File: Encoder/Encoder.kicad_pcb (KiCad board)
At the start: 2 copper layers, 10 parts, among them J1 Conn_01x04_Socket, J2 Conn_01x04_Socket

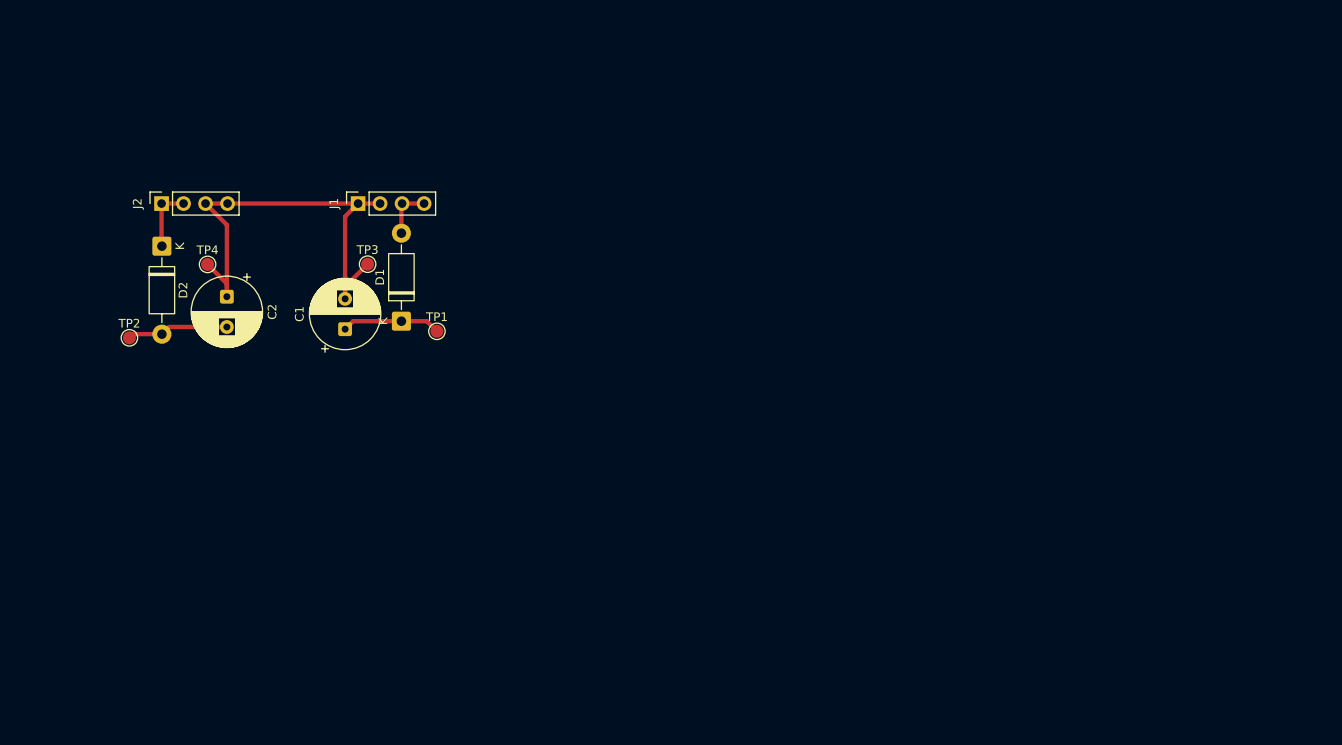
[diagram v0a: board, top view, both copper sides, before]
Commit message: added the filter for L and R
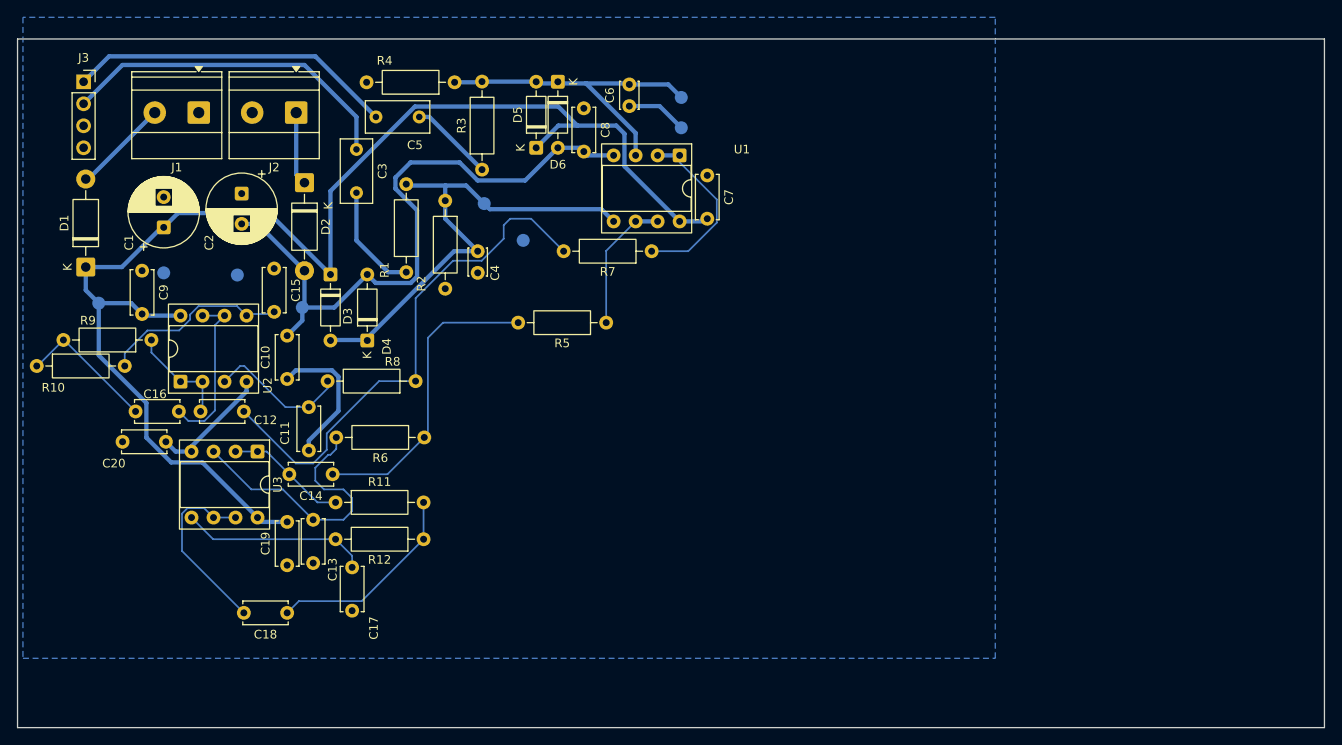
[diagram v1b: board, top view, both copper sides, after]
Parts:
- removed TP1, TP2, TP3, TP4: TestPoint, TestPoint:TestPoint_Pad_D1.5mm
- added C10: 100n, Capacitor_THT:C_Disc_D5.0mm_W2.5mm_P5.00mm, F.Cu at (37.5, 48.2)
- added C11: 1 n, Capacitor_THT:C_Disc_D5.0mm_W2.5mm_P5.00mm, F.Cu at (40.0, 56.5)
- added C12: 1 n, Capacitor_THT:C_Disc_D5.0mm_W2.5mm_P5.00mm, F.Cu at (32.5, 52.0)
- added C13: 1 n, Capacitor_THT:C_Disc_D5.0mm_W2.5mm_P5.00mm, F.Cu at (40.5, 69.5)
- added C14: 1 n, Capacitor_THT:C_Disc_D5.0mm_W2.5mm_P5.00mm, F.Cu at (42.8, 59.2)
- added C15: 330 p, Capacitor_THT:C_Disc_D5.0mm_W2.5mm_P5.00mm, F.Cu at (36.0, 35.5)
- added C16: 2.2 n, Capacitor_THT:C_Disc_D5.0mm_W2.5mm_P5.00mm, F.Cu at (20.0, 52.0)
- added C17: 330 p, Capacitor_THT:C_Disc_D5.0mm_W2.5mm_P5.00mm, F.Cu at (45.0, 75.0)
- added C18: 2.2 n, Capacitor_THT:C_Disc_D5.0mm_W2.5mm_P5.00mm, F.Cu at (37.5, 75.2)
- added C19: 100n, Capacitor_THT:C_Disc_D5.0mm_W2.5mm_P5.00mm, F.Cu at (37.5, 69.8)
- added C20: 100n, Capacitor_THT:C_Disc_D5.0mm_W2.5mm_P5.00mm, F.Cu at (18.5, 55.5)
- added C3: 1u, Capacitor_THT:C_Rect_L7.2mm_W3.5mm_P5.00mm, F.Cu at (45.5, 21.8)
- added C4: 100p, Capacitor_THT:C_Disc_D3.0mm_W2.0mm_P2.50mm, F.Cu at (59.5, 36.0)
- added C5: 1u, Capacitor_THT:C_Rect_L7.2mm_W3.5mm_P5.00mm, F.Cu at (47.8, 18.0)
- added C6: 100p, Capacitor_THT:C_Disc_D3.0mm_W2.0mm_P2.50mm, F.Cu at (77.0, 16.8)
- added C7: 100n, Capacitor_THT:C_Disc_D5.0mm_W2.5mm_P5.00mm, F.Cu at (86.0, 24.8)
- added C8: 100n, Capacitor_THT:C_Disc_D5.0mm_W2.5mm_P5.00mm, F.Cu at (71.8, 17.0)
- added C9: 100n, Capacitor_THT:C_Disc_D5.0mm_W2.5mm_P5.00mm, F.Cu at (20.8, 35.8)
- added D3: 1N4148, Diode_THT:D_DO-35_SOD27_P7.62mm_Horizontal, F.Cu at (42.5, 36.2)
- added D4: 1N4148, Diode_THT:D_DO-35_SOD27_P7.62mm_Horizontal, F.Cu at (46.8, 43.8)
- added D5: 1N4148, Diode_THT:D_DO-35_SOD27_P7.62mm_Horizontal, F.Cu at (66.2, 21.6)
- added D6: 1N4148, Diode_THT:D_DO-35_SOD27_P7.62mm_Horizontal, F.Cu at (68.8, 13.9)
- added J3: Conn_01x04_Socket, Connector_PinSocket_2.54mm:PinSocket_1x04_P2.54mm_Vertical, F.Cu at (14.0, 13.9)
- added R1: 10k, Resistor_THT:R_Axial_DIN0207_L6.3mm_D2.5mm_P10.16mm_Horizontal, F.Cu at (51.2, 35.9)
- added R10: 12k, Resistor_THT:R_Axial_DIN0207_L6.3mm_D2.5mm_P10.16mm_Horizontal, F.Cu at (8.59, 46.8)
- added R11: 12k, Resistor_THT:R_Axial_DIN0207_L6.3mm_D2.5mm_P10.16mm_Horizontal, F.Cu at (43.1, 62.5)
- added R12: 12k, Resistor_THT:R_Axial_DIN0207_L6.3mm_D2.5mm_P10.16mm_Horizontal, F.Cu at (53.2, 66.8)
- added R2: 100k, Resistor_THT:R_Axial_DIN0207_L6.3mm_D2.5mm_P10.16mm_Horizontal, F.Cu at (55.8, 27.7)
- added R3: 10k, Resistor_THT:R_Axial_DIN0207_L6.3mm_D2.5mm_P10.16mm_Horizontal, F.Cu at (60.0, 24.1)
- added R4: 100k, Resistor_THT:R_Axial_DIN0207_L6.3mm_D2.5mm_P10.16mm_Horizontal, F.Cu at (56.8, 14.0)
- added R5: 10k, Resistor_THT:R_Axial_DIN0207_L6.3mm_D2.5mm_P10.16mm_Horizontal, F.Cu at (74.3, 41.8)
- added R6: 10k, Resistor_THT:R_Axial_DIN0207_L6.3mm_D2.5mm_P10.16mm_Horizontal, F.Cu at (53.3, 55.0)
- added R7: 10k, Resistor_THT:R_Axial_DIN0207_L6.3mm_D2.5mm_P10.16mm_Horizontal, F.Cu at (79.6, 33.5)
- added R8: 10k, Resistor_THT:R_Axial_DIN0207_L6.3mm_D2.5mm_P10.16mm_Horizontal, F.Cu at (52.3, 48.5)
- added R9: 12k, Resistor_THT:R_Axial_DIN0207_L6.3mm_D2.5mm_P10.16mm_Horizontal, F.Cu at (21.8, 43.8)
- added TP_+9V1: TestPoint, TestPoint:TestPoint_Pad_D1.5mm, B.Cu at (15.8, 39.5)
- added TP_-9V1: TestPoint, TestPoint:TestPoint_Pad_D1.5mm, B.Cu at (39.2, 40.0)
- added TP_GND1: TestPoint, TestPoint:TestPoint_Pad_D1.5mm, B.Cu at (31.8, 36.2)
- added TP_GND2: TestPoint, TestPoint:TestPoint_Pad_D1.5mm, B.Cu at (64.8, 32.2)
- added TP_GND3: TestPoint, TestPoint:TestPoint_Pad_D1.5mm, B.Cu at (23.2, 36.0)
- added TP_GND4: TestPoint, TestPoint:TestPoint_Pad_D1.5mm, B.Cu at (83.0, 19.2)
- added TP_L1: TestPoint, TestPoint:TestPoint_Pad_D1.5mm, B.Cu at (83.0, 15.8)
- added TP_R1: TestPoint, TestPoint:TestPoint_Pad_D1.5mm, B.Cu at (60.2, 28.0)
- added U1: TL072, Package_DIP:DIP-8_W7.62mm_Socket, F.Cu at (82.8, 22.4)
- added U2: TL072, Package_DIP:DIP-8_W7.62mm_Socket, F.Cu at (25.2, 48.6)
- added U3: TL072, Package_DIP:DIP-8_W7.62mm_Socket, F.Cu at (34.1, 56.6)
- J1, J2: value Conn_01x04_Socket -> Conn_01x02_Socket; footprint Connector_PinSocket_2.54mm:PinSocket_1x04_P2.54mm_Vertical -> TerminalBlock_Phoenix:TerminalBlock_Phoenix_MKDS-1,5-2-5.08_1x02_P5.08mm_Horizontal
- moved D1 37.0 mm to (14.2, 35.3)
- moved C1 24.0 mm to (23.2, 30.8)
- moved J1 21.2 mm to (27.3, 17.5), turned to 180 degrees
- moved J2 18.8 mm to (38.5, 17.5), turned to 180 degrees
- moved D2 18.0 mm to (39.5, 25.6)
- moved C2 12.0 mm to (32.2, 26.8)
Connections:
- J1 pad 2: GND -> Net-(D1-A)
- J2 pad 2: Net-(D2-K) -> GND
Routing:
- net +9V: track 11.5 -> 157.5 mm
- net -9V: track 11.8 -> 88.7 mm
- net Net-(C12-Pad1): track 0.00 -> 60.3 mm
- net /right: track 0.00 -> 56.3 mm
- net Net-(J3-Pin_2): track 0.00 -> 39.6 mm
- net Net-(J3-Pin_1): track 0.00 -> 37.9 mm
- net /left: track 0.00 -> 37.7 mm
- net Net-(C14-Pad1): track 0.00 -> 35.2 mm
- net Net-(U3A-+): track 0.00 -> 32.4 mm
- net GND: track 53.3 -> 23.6 mm
- net Net-(C18-Pad1): track 0.00 -> 23.5 mm
- net Net-(U2B-+): track 0.00 -> 22.1 mm
- net Net-(U3B-+): track 0.00 -> 21.7 mm
- net Net-(U3B--): track 0.00 -> 21.3 mm
- net Net-(U1A--): track 0.00 -> 21.0 mm
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- added copper zone on B.Cu, net GND
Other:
- board outline added: 150.9 x 79.5 mm

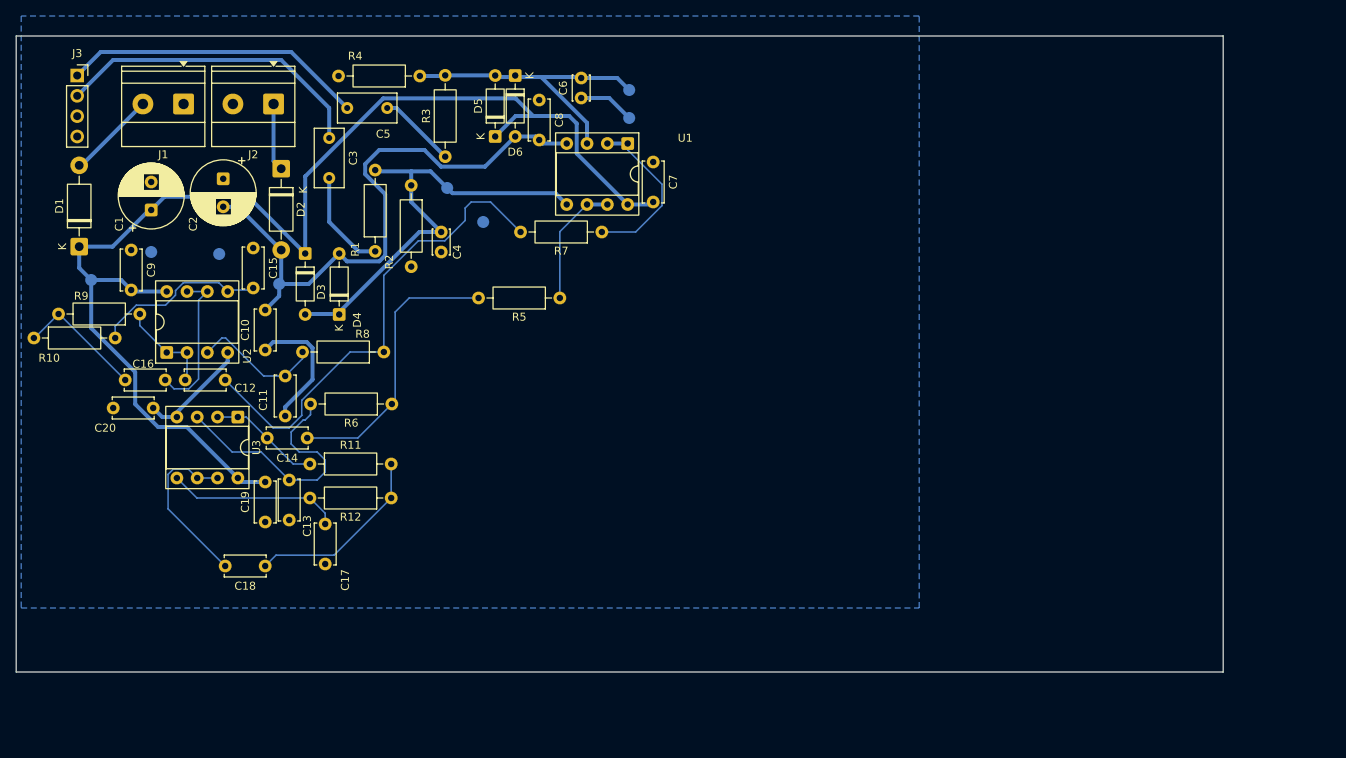
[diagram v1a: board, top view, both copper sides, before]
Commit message: added the filter for L and R
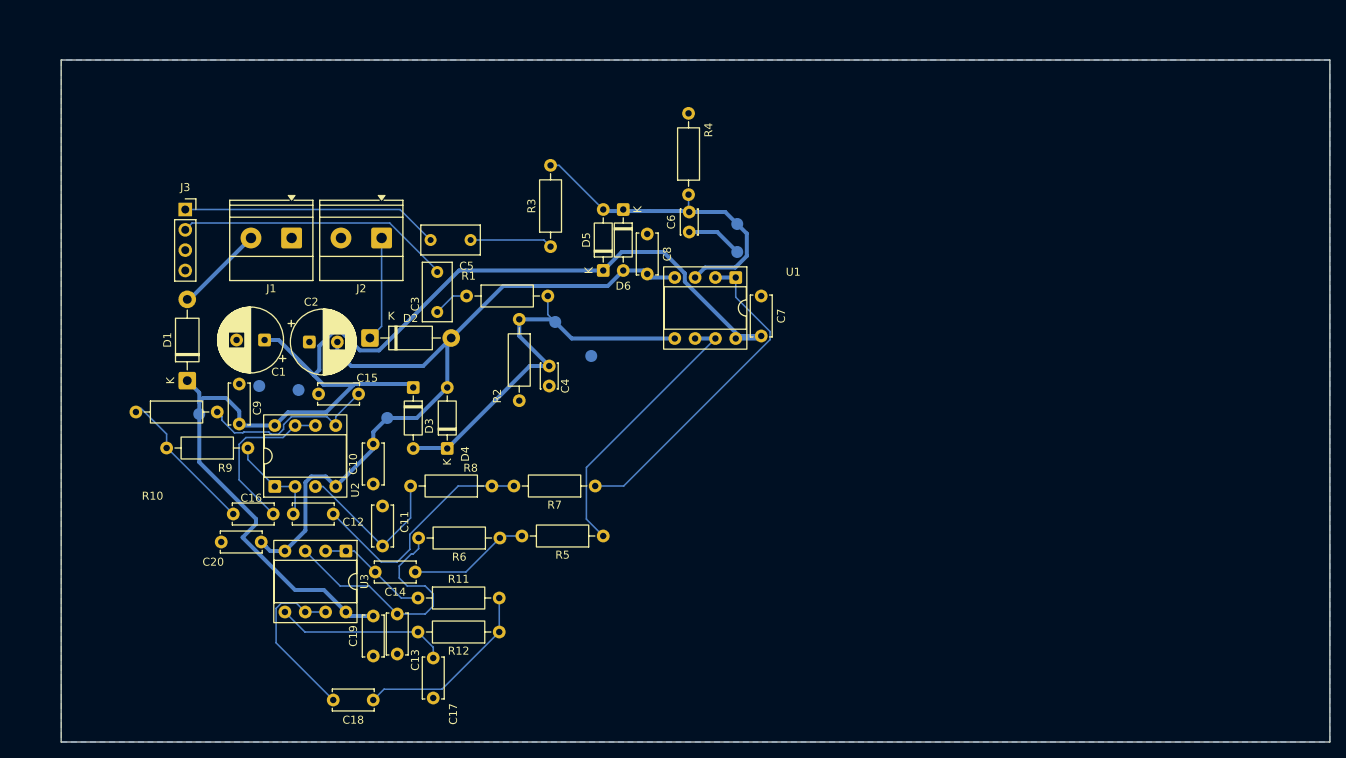
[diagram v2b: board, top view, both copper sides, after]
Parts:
- moved R4 36.7 mm to (90.4, 28.8), turned to 90 degrees
- moved R7 31.8 mm to (78.8, 65.2)
- moved R5 30.2 mm to (79.8, 71.5)
- moved D2 23.9 mm to (50.6, 46.8), turned to 0 degrees
- moved C2 23.1 mm to (43.0, 47.2), turned to 0 degrees
- moved C1 21.6 mm to (37.4, 47.0), turned to 180 degrees
- moved C10 21.5 mm to (51.0, 65.0)
- moved C12 21.5 mm to (46.0, 68.8)
- moved C13 21.5 mm to (54.0, 86.2)
- moved C14 21.5 mm to (56.3, 76.0)
- moved C16 21.5 mm to (33.5, 68.8)
- moved C17 21.5 mm to (58.5, 91.8)
- moved C18 21.5 mm to (51.0, 92.0)
- moved C19 21.5 mm to (51.0, 86.5)
- moved C20 21.5 mm to (32.0, 72.2)
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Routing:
- net Net-(C12-Pad1): track 60.3 -> 30.1 mm
- net Net-(U1A--): track 21.0 -> 41.5 mm
- net Net-(C14-Pad1): track 35.2 -> 15.2 mm
- net Net-(U1B--): track 15.6 -> 34.8 mm
- net GND: track 23.6 -> 7.04 mm
- net Net-(C3-Pad2): track 12.8 -> 4.49 mm
- net +9V: track 157.5 -> 163.6 mm
- net -9V: track 88.7 -> 94.5 mm
- net Net-(J3-Pin_1): track 37.9 -> 32.2 mm
- net Net-(J3-Pin_2): track 39.6 -> 34.5 mm
- net Net-(D2-K): track 8.49 -> 13.1 mm
- net Net-(U2A-+): track 16.3 -> 20.4 mm
- net /right: track 56.3 -> 52.8 mm
- net /left: track 37.7 -> 40.7 mm
- net Net-(C16-Pad1): track 16.1 -> 18.1 mm
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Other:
- board size 150.9 x 79.5 mm -> 158.6 x 85.2 mm

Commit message: new board layout
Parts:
- removed C17: 330 p, Capacitor_THT:C_Disc_D5.0mm_W2.5mm_P5.00mm
- removed C18: 2.2 n, Capacitor_THT:C_Disc_D5.0mm_W2.5mm_P5.00mm
- removed TP_GND2, TP_R1: TestPoint, TestPoint:TestPoint_Pad_D1.5mm
- added C21: 100n, Capacitor_THT:C_Disc_D5.0mm_W2.5mm_P5.00mm, F.Cu at (79.9, 27.0)
- added C22: 100n, Capacitor_THT:C_Disc_D5.0mm_W2.5mm_P5.00mm, F.Cu at (96.2, 36.8)
- added R13: 100k, Resistor_THT:R_Axial_DIN0207_L6.3mm_D2.5mm_P10.16mm_Horizontal, F.Cu at (100.6, 50.4)
- added R14: 100k, Resistor_THT:R_Axial_DIN0207_L6.3mm_D2.5mm_P10.16mm_Horizontal, F.Cu at (104.1, 57.8)
- added R15: 100k, Resistor_THT:R_Axial_DIN0207_L6.3mm_D2.5mm_P10.16mm_Horizontal, F.Cu at (107.4, 47.9)
- added R16: 100k, Resistor_THT:R_Axial_DIN0207_L6.3mm_D2.5mm_P10.16mm_Horizontal, F.Cu at (92.1, 45.8)
- added R17: 100k, Resistor_THT:R_Axial_DIN0207_L6.3mm_D2.5mm_P10.16mm_Horizontal, F.Cu at (91.5, 43.1)
- added R18: 100k, Resistor_THT:R_Axial_DIN0207_L6.3mm_D2.5mm_P10.16mm_Horizontal, F.Cu at (83.2, 26.8)
- added TP_GND5: TestPoint, TestPoint:TestPoint_Pad_D1.5mm, B.Cu at (113.8, 55.0)
- added TP_L2: TestPoint, TestPoint:TestPoint_Pad_D1.5mm, B.Cu at (96.9, 50.0)
- added U4: TL072, Package_DIP:DIP-8_W7.62mm_Socket, F.Cu at (80.8, 42.4)
- added U7: TL072, Package_DIP:DIP-8_W7.62mm_Socket, F.Cu at (33.8, 77.9)
- moved C19 70.3 mm to (26.9, 20.5), turned to -90 degrees
- moved R11 69.9 mm to (23.8, 17.5)
- moved R5 65.8 mm to (24.2, 36.2)
- moved R6 65.6 mm to (14.0, 32.8), turned to 0 degrees
- moved C14 61.0 mm to (18.9, 27.8), turned to 0 degrees
- moved TP_L1 57.8 mm to (45.2, 59.2), turned to 180 degrees
- moved R4 55.8 mm to (42.2, 57.1)
- moved R3 55.3 mm to (25.3, 63.0), turned to 0 degrees
- moved C9 54.9 mm to (88.9, 58.2), turned to 90 degrees
- moved R10 54.5 mm to (75.8, 53.0)
- moved U2 53.6 mm to (92.1, 61.0)
- moved R12 53.6 mm to (74.1, 30.4), turned to -90 degrees
- moved TP_GND4 52.9 mm to (65.4, 78.8), turned to 180 degrees
- moved C13 51.6 mm to (39.4, 36.8)
- moved C4 51.4 mm to (23.1, 40.5), turned to 0 degrees
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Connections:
- C11 pad 2: Net-(U2A-+) -> Net-(U1B-+)
- C12 pad 2: Net-(U2A--) -> Net-(U1B--)
- C13 pad 2: Net-(U3A-+) -> Net-(U3B-+)
- C14 pad 2: Net-(U3A--) -> Net-(U3B--)
- R11 pad 1: Net-(U3A--) -> Net-(U3B--)
- R12 pad 2: Net-(U3B-+) -> Net-(U2A-+)
- R5 pad 1: Net-(U1B--) -> Net-(U3A--)
- R6 pad 2: Net-(U3A-+) -> Net-(U3B-+)
- R8 pad 2: Net-(U2A-+) -> Net-(U1B-+)
- R9 pad 1: Net-(U2A--) -> Net-(U1B--)
- U1 pad 5: /right -> Net-(U1B-+)
- U3 pad 3: Net-(U3A-+) -> /right
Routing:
- net -9V: track 94.5 -> 183.9 mm
- net /right: track 52.8 -> 18.5 mm
- net Net-(U3A-+): track 32.4 -> 0.00 mm
- net Net-(U4A--): track 0.00 -> 31.2 mm
- net +9V: track 163.6 -> 194.7 mm
- net Net-(U4A-+): track 0.00 -> 29.7 mm
- net Net-(U4B--): track 0.00 -> 29.1 mm
- net Net-(J3-Pin_1): track 32.2 -> 3.51 mm
- net Net-(U1A--): track 41.5 -> 15.4 mm
- net Net-(C12-Pad1): track 30.1 -> 7.74 mm
- net Net-(C18-Pad1): track 23.5 -> 45.5 mm
- net Net-(J3-Pin_2): track 34.5 -> 13.1 mm
- net Net-(R16-Pad2): track 0.00 -> 19.8 mm
- net Net-(U1B-+): track 0.00 -> 15.8 mm
- net Net-(R18-Pad2): track 0.00 -> 15.5 mm
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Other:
- board size 158.6 x 85.2 mm -> 150 x 100 mm
